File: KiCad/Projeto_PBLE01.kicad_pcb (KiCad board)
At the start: 2 copper layers, 78 parts, among them IC1 LM358

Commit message: começo da pcb
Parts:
- added Ganho_AO_1: SW_DIP_x04, My_Lib:DIP4PIN, F.Cu at (88.5, 170.5)
- added Ganho_AO_2: SW_DIP_x04, My_Lib:DIP4PIN, F.Cu at (74.6, 170.7)
- added Led_Control1: SW_DIP_x04, My_Lib:DIP4PIN, F.Cu at (110.0, 140.8)
- added PWR_Source1: Jack-DC, My_Lib:PJ-002A, F.Cu at (53.2, 127.1)
- added Retificador_de_tensão_5v1: LD1117DT50TR, My_Lib:LD1117DT50TR, F.Cu at (74.5, 116.2)
- added SW_POT1: SW_DIP_x01, My_Lib:DIP1PIN, F.Cu at (61.7, 146.2)
- D1, D3, D4, D_PWR_GREEN1, Escrita_USB1, Leitura_USB1: footprint LED_SMD:LED_1206_3216Metric -> LED_SMD:LED_1206_3216Metric_Pad1.42x1.75mm_HandSolder
- D2: footprint LED_SMD:LED_1206_3216Metric_Castellated -> LED_SMD:LED_1206_3216Metric_Pad1.42x1.75mm_HandSolder
- POT1: footprint LED_SMD:LED_2010_5025Metric -> Potentiometer_THT:Potentiometer_Piher_T-16H_Single_Horizontal
- Reset_Button1: footprint Resistor_SMD:R_0805_2012Metric -> Button_Switch_THT:SW_PUSH_6mm
- moved B0 503.0 mm to (73.1, 148.5)
- moved Source_Pins1 494.4 mm to (130.2, 153.3), turned to 180 degrees
- moved R_B3 482.2 mm to (101.4, 145.0)
- moved R_B1 482.0 mm to (81.4, 145.2)
- moved B1 480.4 mm to (83.0, 148.5)
- moved D3 480.1 mm to (92.2, 137.5)
- moved D4 479.8 mm to (92.2, 140.9)
- moved IO_Pins1 479.3 mm to (129.5, 138.4), turned to 180 degrees
- moved B3 477.6 mm to (102.8, 148.5)
- moved R_B4 475.2 mm to (111.4, 145.4)
- moved R_B2 473.8 mm to (91.2, 145.3)
- moved R_LED_2 472.0 mm to (97.3, 134.2)
- moved R_B0 471.2 mm to (73.2, 144.9), turned to 270 degrees
- moved B2 470.9 mm to (93.0, 148.5)
- moved C_Reset1 468.1 mm to (69.7, 117.4), turned to 270 degrees
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
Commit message: componentes pbc
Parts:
- moved R2_30k_AO_2 117.2 mm to (125.4, 86.6), turned to 90 degrees
- moved R2_10k_AO_2 109.8 mm to (128.2, 86.8), turned to 270 degrees
- moved R2_30k_3_AO_2 109.2 mm to (120.6, 86.6), turned to 90 degrees
- moved R2_30k_2_AO_2 105.2 mm to (122.9, 86.8), turned to 90 degrees
- moved R2_30k_3_AO_1 100.9 mm to (100.0, 86.9), turned to 270 degrees
- moved R2_10k_AO_1 99.2 mm to (107.4, 87.0), turned to 270 degrees
- moved R2_30k_AO_1 96.7 mm to (104.9, 86.9), turned to 270 degrees
- moved R2_30k_2_AO_1 95.4 mm to (102.4, 86.9), turned to 270 degrees
- moved Ganho_AO_2 93.8 mm to (126.2, 92.3), turned to 180 degrees
- moved R1_AO_2 88.8 mm to (129.0, 100.5), turned to 180 degrees
- moved IC1 84.9 mm to (112.4, 106.2)
- moved R1_AO_1 83.2 mm to (116.2, 113.6)
- moved Ganho_AO_1 81.9 mm to (113.2, 92.5), turned to 180 degrees
- moved C2_Retificador1 78.8 mm to (75.7, 113.0), turned to 270 degrees
- moved R2 76.3 mm to (114.2, 132.3), turned to 90 degrees
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
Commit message: Trilhas
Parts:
- moved R2_10k_AO2 7.24 mm to (129.4, 93.9), turned to 90 degrees
- moved Cristal_32KHZ 4.29 mm to (81.3, 132.7), turned to 0 degrees
- moved R2_30k_2_AO1 4.14 mm to (98.4, 88.1), turned to 180 degrees
- moved C1 3.99 mm to (67.8, 93.2)
- moved C2 3.99 mm to (72.6, 93.2)
- moved Cref1 3.76 mm to (80.4, 85.1)
- moved C2_Ret 3.72 mm to (73.8, 109.8)
- moved Cref0 3.65 mm to (80.4, 88.7)
- moved R1_AO_1 3.55 mm to (112.7, 112.8)
- moved R_D_2 3.42 mm to (95.4, 132.6)
- moved R_D_1 3.39 mm to (95.3, 129.0)
- moved R_RST 3.37 mm to (68.6, 104.0)
- moved R_D_3 3.32 mm to (95.4, 136.2)
- moved R_D_4 3.27 mm to (95.4, 139.8)
- moved Source 3.18 mm to (129.5, 150.3)
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- renumbered Filtro_Butterworth1 to Butterworth, C1_Cristal_12 to C1, C1_Retificador1 to C1_Ret, C2__Cristal_12 to C2, C2_Retificador1 to C2_Ret, CX1_20MHz1 to CX1, CX2_20MHz1 to CX2, C_GND_Filtro1 to C_FiltroB, C_Reset1 to C_Reset, C_Reset_Conversor1 to C_Reset_Conversor, C_Vcc_timer1 to C_Vcc_timer, Conversor_UART_USB1 to Conversor_UART, Cristal_20MHz1 to Cristal_20MHz, Cristal-AB26T-32.768KHZ1 to Cristal_32KHZ, Crystal_12MHz1 to Crystal_12MHz, D_Schottky1 to D_Schottky, IC1 to IC, LCD1 to LCD, MCU1 to MCU, POT1 to POT, D_PWR_GREEN1 to PWR_GREEN, PWR_Source1 to PWR_Source, Porta_USB1 to Porta_USB, Potenciometro_10k1 to Pot_LCD, R_LED_USB_R1 to R1_USB_R, R2_10k_AO_1 to R2_10k_AO1, R2_10k_AO_2 to R2_10k_AO2, R2_30k_2_AO_1 to R2_30k_2_AO1, R2_30k_2_AO_2 to R2_30k_2_AO2, R2_30k_3_AO_1 to R2_30k_3_AO1, R2_30k_3_AO_2 to R2_30k_3_AO2, R2_30k_AO_1 to R2_30k_AO1, R2_30k_AO_2 to R2_30k_AO2, R_LED_USB_R2 to R2_USB_R, R_CLK1 to R_CLK, R_DATA1 to R_DATA, R_LED_1 to R_D_1, R_LED_2 to R_D_2, R_LED_3 to R_D_3, R_LED_4 to R_D_4, R_Filtro_In-1 to R_FiltroB, G_LED_PWR1 to R_LED_PWR, R_MFP1 to R_MFP, R_RST1 to R_RST, R_Reset1 to R_Reset, Leitura_USB1 to R_USB, Reset_Button1 to Reset_Button, Retificador_de_tensão_5v1 to Ret5V, SW_POT1 to SW_POT, Source_Pins1 to Source, Timer_externo1 to Timer, Escrita_USB1 to W_USB
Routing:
- net GNDREF: track 0.00 -> 474.3 mm
- net Vcc_5v: track 0.00 -> 284.8 mm, vias 0 -> 1
- net /Analog_1: track 0.00 -> 73.0 mm, vias 0 -> 1
- net /Analog_0: track 0.00 -> 66.2 mm, vias 0 -> 1
- net /ICSP_Enable: track 0.00 -> 63.4 mm
- net /IO_00: track 0.00 -> 57.4 mm, vias 0 -> 1
- net /IO_01: track 0.00 -> 57.0 mm, vias 0 -> 1
- net /ICSP_Clk: track 0.00 -> 56.9 mm
- net /ICSP_Data: track 0.00 -> 56.1 mm
- net /MCLR: track 0.00 -> 53.3 mm, vias 0 -> 1
- net /IO_03: track 0.00 -> 51.8 mm
- net /LCD_RS: track 0.00 -> 51.2 mm, vias 0 -> 1
- net /Analog_KB: track 0.00 -> 49.3 mm, vias 0 -> 1
- net /ICSP_RST: track 0.00 -> 49.3 mm, vias 0 -> 1
- net /LCD_RW: track 0.00 -> 49.2 mm, vias 0 -> 1
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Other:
- board outline added: 80 x 80 mm
- rule via_min_size: 0.4 -> 0.6
- board text added: "GND"

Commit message: adição do plano de terra e furos de fixação
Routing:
- net (no net): vias 0 -> 2
- added copper zone on B.Cu, net GNDREF

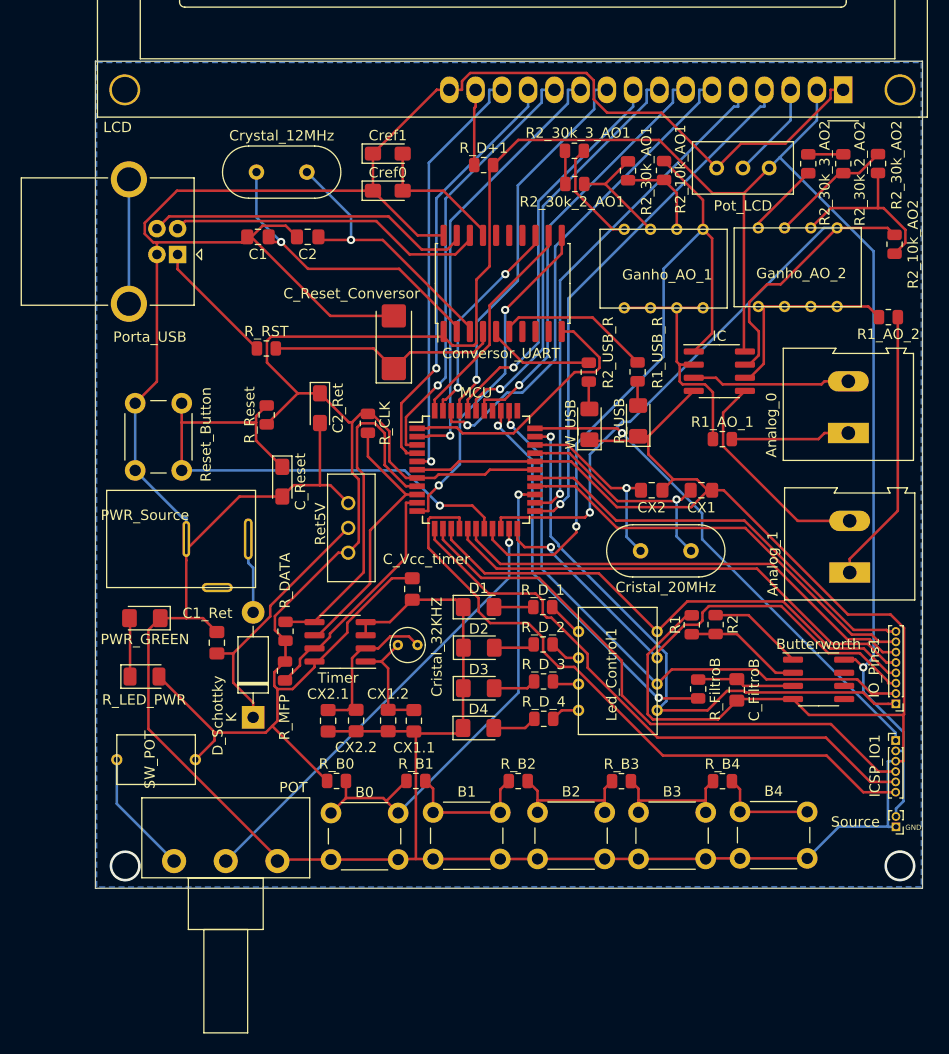
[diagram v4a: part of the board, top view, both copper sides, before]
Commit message: PCB resolução dos erros
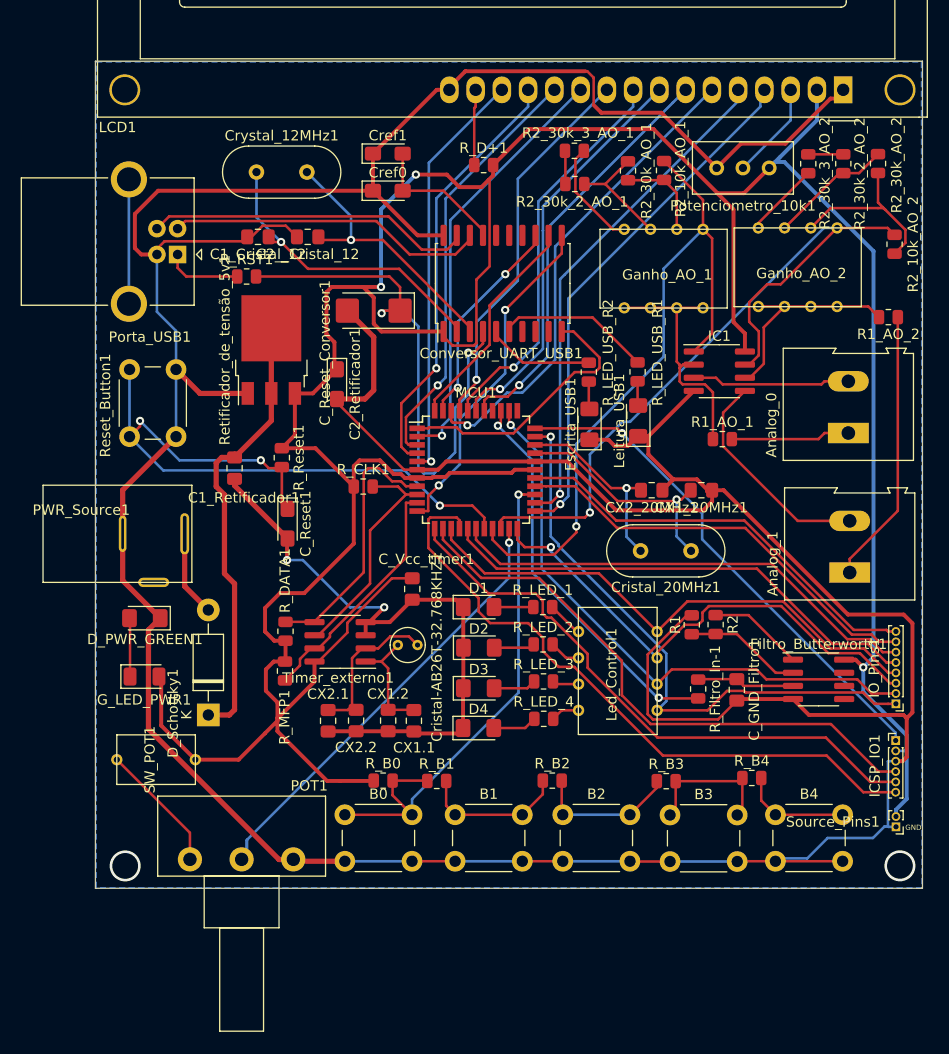
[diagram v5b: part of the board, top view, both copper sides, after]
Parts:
- Retificador_de_tensão_5v1: renamed from Ret5V; footprint My_Lib:LD1117DT50TR -> Package_TO_SOT_SMD:TO-252-3_TabPin2
- moved C1_Retificador1 17.0 mm to (65.5, 115.6), turned to 270 degrees
- moved Retificador_de_tensão_5v1 13.2 mm to (69.1, 104.1), turned to 90 degrees
- moved R_RST1 7.22 mm to (66.7, 97.0)
- moved PWR_Source1 6.17 mm to (47.0, 126.6)
- moved R_CLK1 6.13 mm to (78.0, 117.3), turned to 0 degrees
- moved Reset_Button1 5.99 mm to (55.4, 112.5), turned to 90 degrees
- moved R_B0 4.51 mm to (79.9, 145.8)
- moved R_Reset1 4.39 mm to (70.1, 114.6), turned to 270 degrees
- moved D_Schottky1 4.34 mm to (63.0, 139.4)
- moved R_B3 4.33 mm to (107.3, 145.8)
- moved C_Reset1 4.10 mm to (70.7, 120.9)
- moved C_Reset_Conversor1 3.63 mm to (79.0, 100.3), turned to 180 degrees
- moved B4 3.44 mm to (117.9, 149.1)
- moved R_B2 3.29 mm to (96.3, 145.8)
- moved B3 3.06 mm to (107.7, 149.1)
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- renumbered C1 to C1_Cristal_12, C1_Ret to C1_Retificador1, C2_Ret to C2_Retificador1, C2 to C2__Cristal_12, CX1 to CX1_20MHz1, CX2 to CX2_20MHz1, C_FiltroB to C_GND_Filtro1, C_Reset to C_Reset1, C_Reset_Conversor to C_Reset_Conversor1, C_Vcc_timer to C_Vcc_timer1, Conversor_UART to Conversor_UART_USB1, Cristal_32KHZ to Cristal-AB26T-32.768KHZ1, Cristal_20MHz to Cristal_20MHz1, Crystal_12MHz to Crystal_12MHz1, PWR_GREEN to D_PWR_GREEN1, D_Schottky to D_Schottky1, W_USB to Escrita_USB1, Butterworth to Filtro_Butterworth1, R_LED_PWR to G_LED_PWR1, IC to IC1, LCD to LCD1, R_USB to Leitura_USB1, MCU to MCU1, POT to POT1, PWR_Source to PWR_Source1, Porta_USB to Porta_USB1, Pot_LCD to Potenciometro_10k1, R2_10k_AO1 to R2_10k_AO_1, R2_10k_AO2 to R2_10k_AO_2, R2_30k_2_AO1 to R2_30k_2_AO_1, R2_30k_2_AO2 to R2_30k_2_AO_2, R2_30k_3_AO1 to R2_30k_3_AO_1, R2_30k_3_AO2 to R2_30k_3_AO_2, R2_30k_AO1 to R2_30k_AO_1, R2_30k_AO2 to R2_30k_AO_2, R_CLK to R_CLK1, R_DATA to R_DATA1, R_FiltroB to R_Filtro_In-1, R_D_1 to R_LED_1, R_D_2 to R_LED_2, R_D_3 to R_LED_3, R_D_4 to R_LED_4, R1_USB_R to R_LED_USB_R1, R2_USB_R to R_LED_USB_R2, R_MFP to R_MFP1, R_RST to R_RST1, R_Reset to R_Reset1, Reset_Button to Reset_Button1, SW_POT to SW_POT1, Source to Source_Pins1, Timer to Timer_externo1
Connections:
- PWR_Source1 pad 3: (no net) -> GNDREF
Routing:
- net Vcc_5v: track 284.8 -> 322.0 mm, vias 1 -> 3
- net Net-(C_Reset_Conversor1-Pad1): track 23.0 -> 54.3 mm, vias 0 -> 2
- net Net-(C1_Retificador1-Pad1): track 25.3 -> 43.8 mm
- net GNDREF: track 474.3 -> 489.0 mm, vias 0 -> 2
- net /MCLR: track 53.3 -> 67.0 mm, vias 1 -> 3
- net /Serial_Data: track 34.2 -> 25.3 mm
- net /Vbus_Externo: track 12.3 -> 7.40 mm
- net /Serial_Clk: track 26.1 -> 22.1 mm
- net VCC: track 7.29 -> 10.8 mm
- net /LCD_B4: track 42.6 -> 41.0 mm
- net /Analog_KB: track 49.3 -> 50.8 mm
- net /LCD_ENABLE: track 47.0 -> 48.3 mm
- net /LCD_RW: track 49.2 -> 48.0 mm
- net /Analog_2: track 43.5 -> 44.8 mm
- net Net-(B1-Pad1): track 13.2 -> 14.3 mm
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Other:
- net class Default: clearance 0.2 -> 0
- rule trace_clearance: 0.2 -> 0

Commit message: ajuste da PCB
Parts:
- moved Power 0.91 mm to (128.9, 150.9)
- moved IO_Pins1 0.63 mm to (128.9, 138.4)
- moved ICSP 0.61 mm to (128.9, 141.9)
- renumbered ICSP_IO1 to ICSP, Source_Pins1 to Power
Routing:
- net GNDREF: track 489.0 -> 469.5 mm
- net /IO_01: track 57.0 -> 54.7 mm
- net Vcc_5v: track 322.0 -> 324.2 mm
- net /IO_04: track 47.4 -> 46.8 mm
- net /IO_07: track 41.1 -> 40.4 mm
- net /IO_06: track 41.2 -> 40.5 mm
- net /IO_02: track 48.6 -> 48.0 mm
- net /IO_00: track 57.4 -> 56.8 mm
- net /IO_05: track 46.2 -> 45.6 mm
- net /ICSP_Enable: track 63.3 -> 62.7 mm
- net /ICSP_Data: track 56.1 -> 55.5 mm
- net /ICSP_Clk: track 56.9 -> 56.3 mm
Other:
- board text added: "Clk"
- board text added: "Data"
- board text added: "Enb"
- board text added: "Grupo 5"
- board text added: "IO_0"
- board text added: "IO_1"
- board text added: "IO_2"
- board text added: "IO_3"
- board text added: "IO_4"
- board text added: "IO_5"
- board text added: "IO_6"
- board text added: "IO_7"
- board text added: "RST"
- board text added: "Vcc"
- board text added: "ñ"

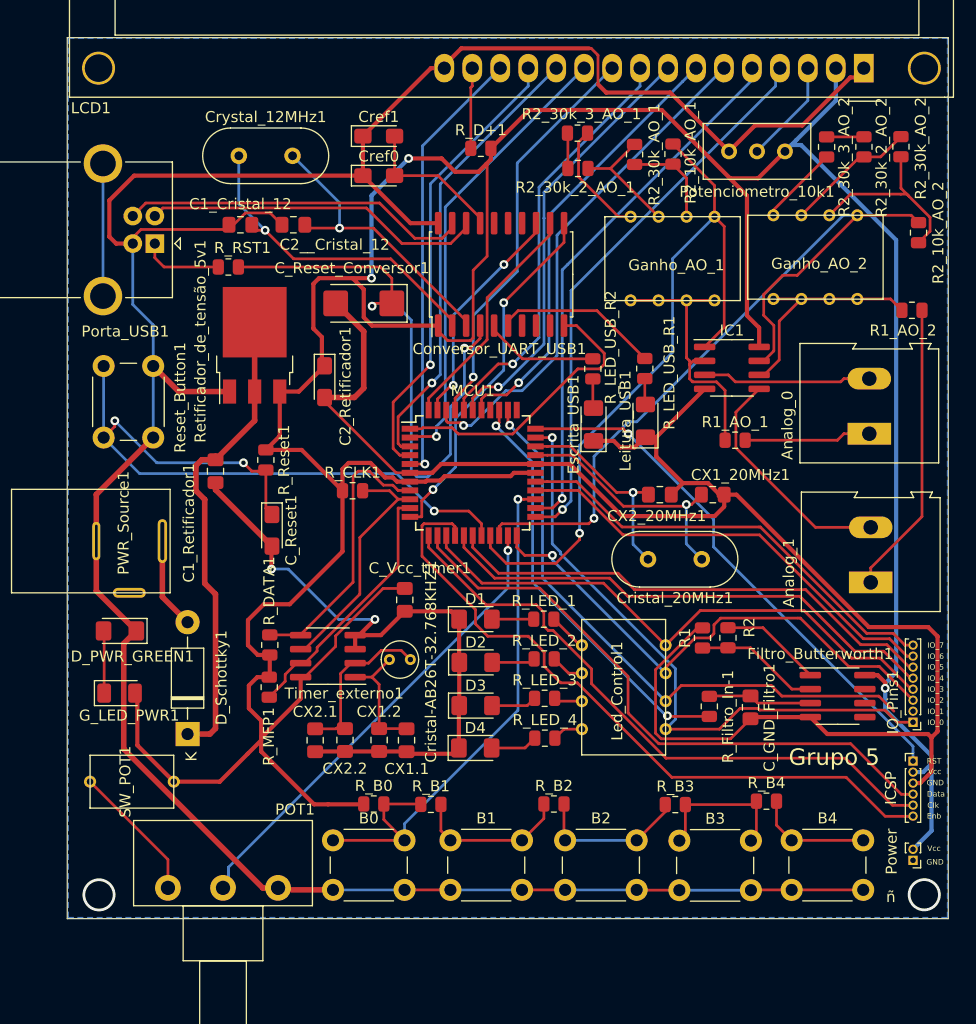
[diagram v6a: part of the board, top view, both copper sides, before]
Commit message: correção P1: LCD e Capacitores
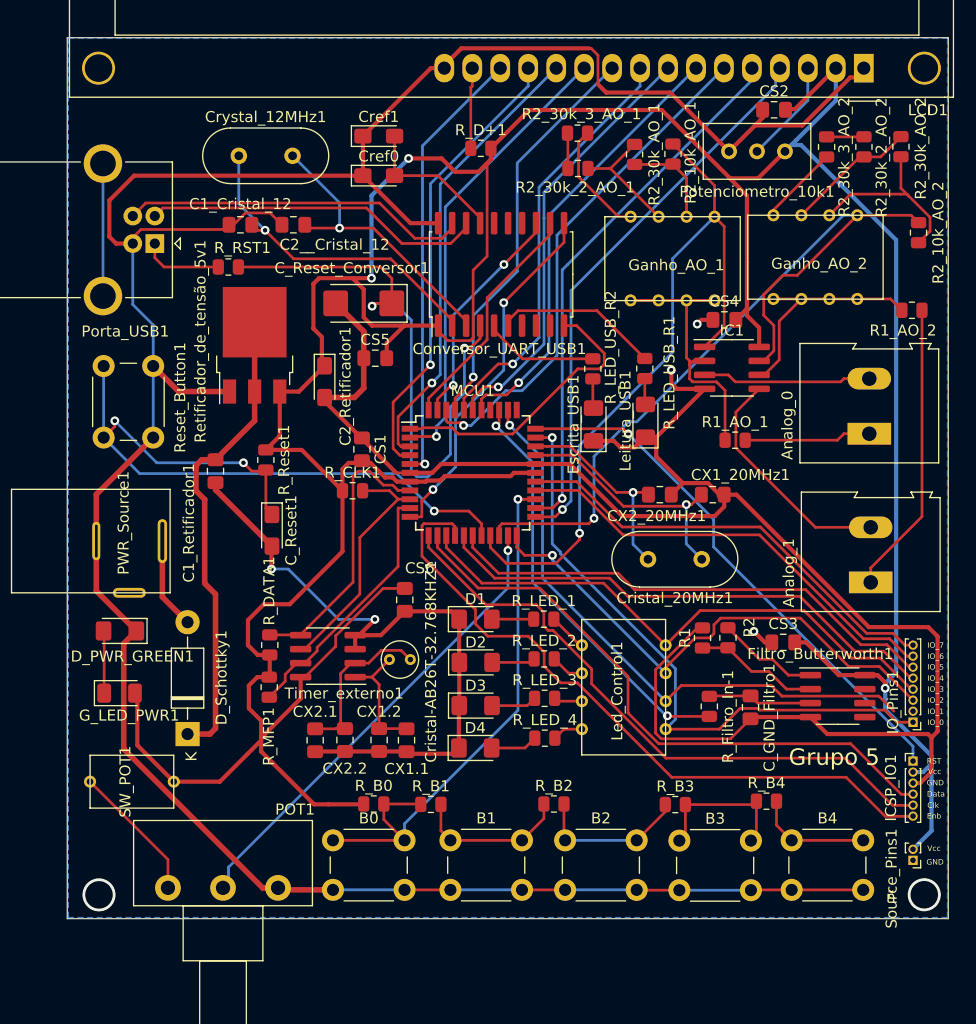
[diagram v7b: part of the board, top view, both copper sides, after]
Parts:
- added CS1: C, Capacitor_SMD:C_0805_2012Metric_Pad1.18x1.45mm_HandSolder, F.Cu at (78.8, 113.6)
- added CS2: C, Capacitor_SMD:C_0805_2012Metric_Pad1.18x1.45mm_HandSolder, F.Cu at (116.3, 82.8)
- added CS3: C, Capacitor_SMD:C_0805_2012Metric_Pad1.18x1.45mm_HandSolder, F.Cu at (117.1, 131.1)
- added CS4: C, Capacitor_SMD:C_0805_2012Metric_Pad1.18x1.45mm_HandSolder, F.Cu at (111.7, 101.8)
- added CS5: C, Capacitor_SMD:C_0805_2012Metric_Pad1.18x1.45mm_HandSolder, F.Cu at (80.0, 105.3)
- renumbered C_Vcc_timer1 to CS6, ICSP to ICSP_IO1, Power to Source_Pins1
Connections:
- PWR_Source1 pad 3: GNDREF -> (no net)
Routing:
- net Vcc_5v: track 324.2 -> 343.0 mm
- net GNDREF: track 469.5 -> 479.4 mm, vias 2 -> 5

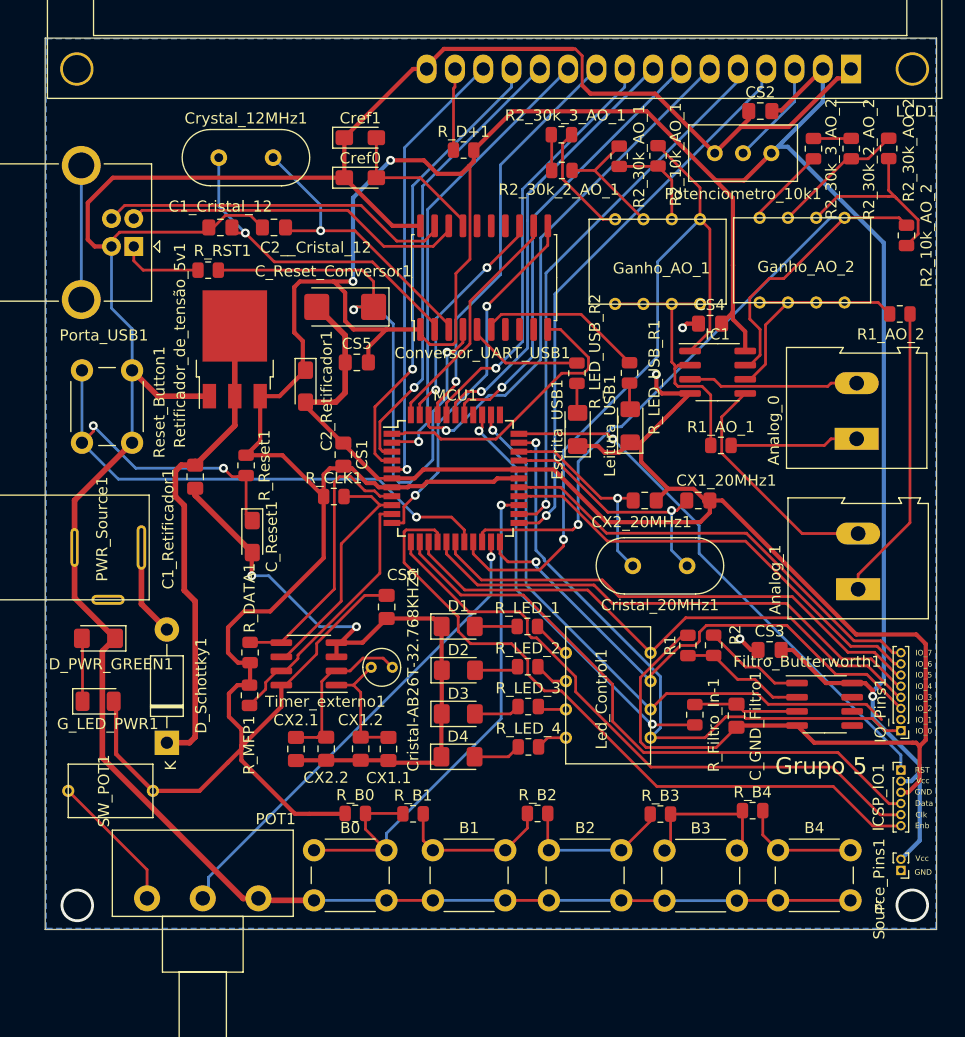
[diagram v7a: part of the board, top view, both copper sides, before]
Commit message: correções de trilha
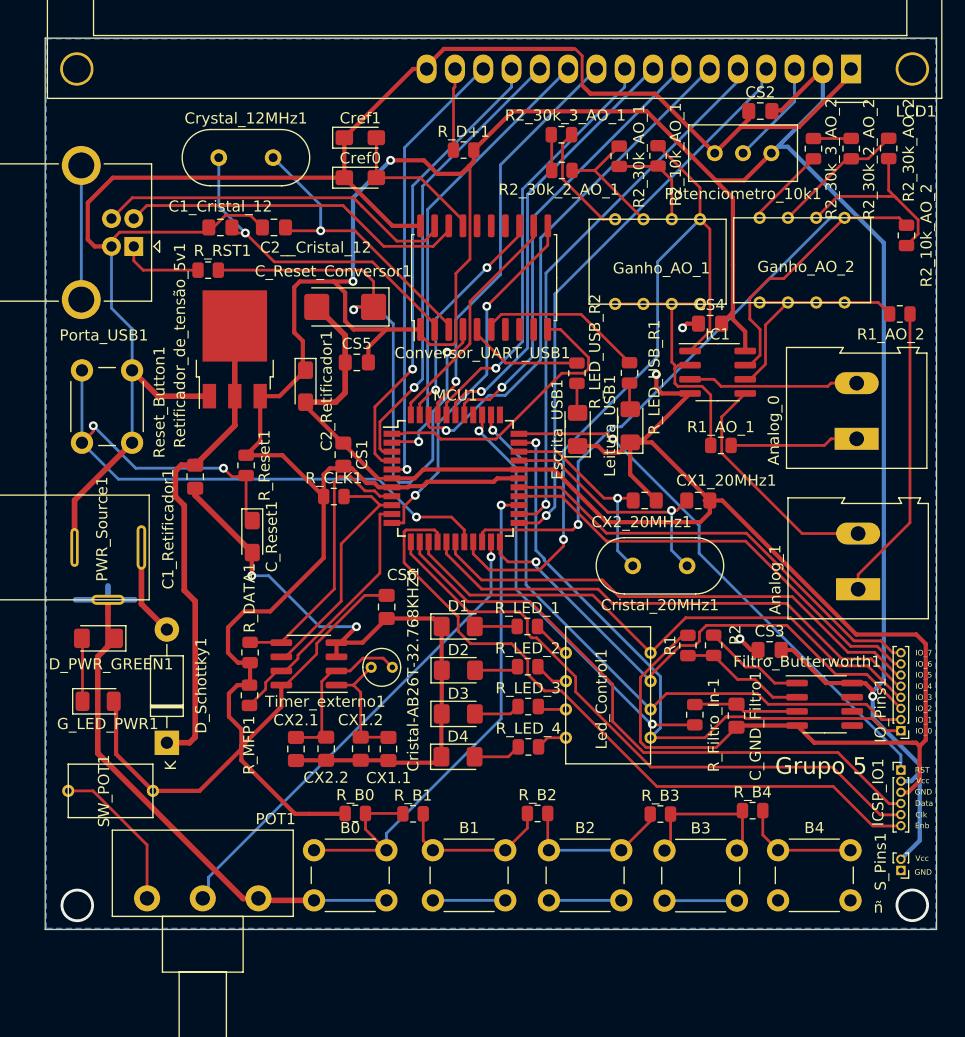
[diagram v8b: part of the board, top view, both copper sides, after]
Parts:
- renumbered Source_Pins1 to S_Pins1
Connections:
- PWR_Source1 pad 3: (no net) -> GNDREF
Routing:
- net GNDREF: track 479.4 -> 465.3 mm
- net /IO_01: track 54.7 -> 56.4 mm
- net Net-(POT1-Pad1): track 12.6 -> 13.9 mm
- net /USB_D+: track 31.7 -> 32.3 mm
- net /IO_06: track 40.5 -> 41.1 mm
